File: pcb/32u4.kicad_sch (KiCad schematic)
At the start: 114 parts, among them J0 USB_C_Receptacle_USB2.0, SW00 SW_SPST, SW01 SW_SPST, SW010 SW_SPST, SW011 SW_SPST, SW02 SW_SPST, SW03 SW_SPST, SW04 SW_SPST, SW05 SW_SPST, SW06 SW_SPST, SW07 SW_SPST, SW08 SW_SPST, SW09 SW_SPST, SW1.0 SW_SPST, SW1.1 SW_SPST, SW110 SW_SPST, SW111 SW_SPST, SW12 SW_SPST, SW13 SW_SPST, SW14 SW_SPST, SW15 SW_SPST, SW16 SW_SPST, SW17 SW_SPST, SW18 SW_SPST, SW19 SW_SPST, SW20 SW_SPST, SW21 SW_SPST, SW210 SW_SPST, SW211 SW_SPST, SW22 SW_SPST, SW23 SW_SPST, SW24 SW_SPST, SW25 SW_SPST, SW26 SW_SPST, SW27 SW_SPST, SW28 SW_SPST, SW29 SW_SPST, SW30 SW_SPST, SW31 SW_SPST, SW310 SW_SPST, SW311 SW_SPST, SW32 SW_SPST, SW33 SW_SPST, SW34 SW_SPST, SW35 SW_SPST, SW36 SW_SPST, SW37 SW_SPST, SW38 SW_SPST, SW39 SW_SPST, SW40 SW_SPST, SW41 SW_SPST, SW411 SW_SPST, SW42 SW_SPST, SW44 SW_SPST, SW45 SW_SPST, SW46 SW_SPST, SW47 SW_SPST, SW49 SW_SPST, U0 ATmega32U4-A, U1 SRV05-4, Y0 Crystal_GND24_Small

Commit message: updated pcb to rp2040
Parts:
- removed C0, C1: 22pf, Capacitor_SMD:C_0805_2012Metric, symbol Device:C_Small
- removed C2: 1uf, Capacitor_SMD:C_0805_2012Metric, symbol Device:C_Small
- removed C3, C4, C6: .1uf / 100nf, Capacitor_SMD:C_0805_2012Metric, symbol Device:C_Small
- removed C5: 10uf, Capacitor_SMD:C_0805_2012Metric, symbol Device:C_Small
- removed F0: Polyfuse, Fuse:Fuse_1206_3216Metric, symbol Device:Polyfuse
- removed J0: USB_C_Receptacle_USB2.0, Connector_USB:USB_C_Receptacle_HRO_TYPE-C-31-M-12, symbol Connector:USB_C_Receptacle_USB2.0
- removed R0: 10k, Resistor_SMD:R_0805_2012Metric, symbol Device:R
- removed R1, R2: 22, Resistor_SMD:R_0805_2012Metric, symbol Device:R_Small
- removed R3, R4: 5.1k, Resistor_SMD:R_0805_2012Metric, symbol Device:R_Small
- removed R5: 10k, Resistor_SMD:R_0805_2012Metric, symbol Device:R_Small
- removed SWRESET1: SW_PUSH, Button_Switch_SMD:SW_SPST_TL3342, symbol keyboard_parts:SW_PUSH
- removed U0: ATmega32U4-A, Package_QFP:TQFP-44_10x10mm_P0.8mm, symbol MCU_Microchip_ATmega:ATmega32U4-A
- removed U1: SRV05-4, Package_TO_SOT_SMD:SOT-23-6, symbol Power_Protection:SRV05-4
- removed Y0: Crystal_GND24_Small, Crystal:Crystal_SMD_3225-4Pin_3.2x2.5mm, symbol Device:Crystal_GND24_Small
- renumbered D0506 to D506, SW010 to SW10, SW011 to SW11
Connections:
- no-connect marks 5 -> 1
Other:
- added sheet Rp2040  (rp2040_temp/RP2040_tmp.kicad_sch)

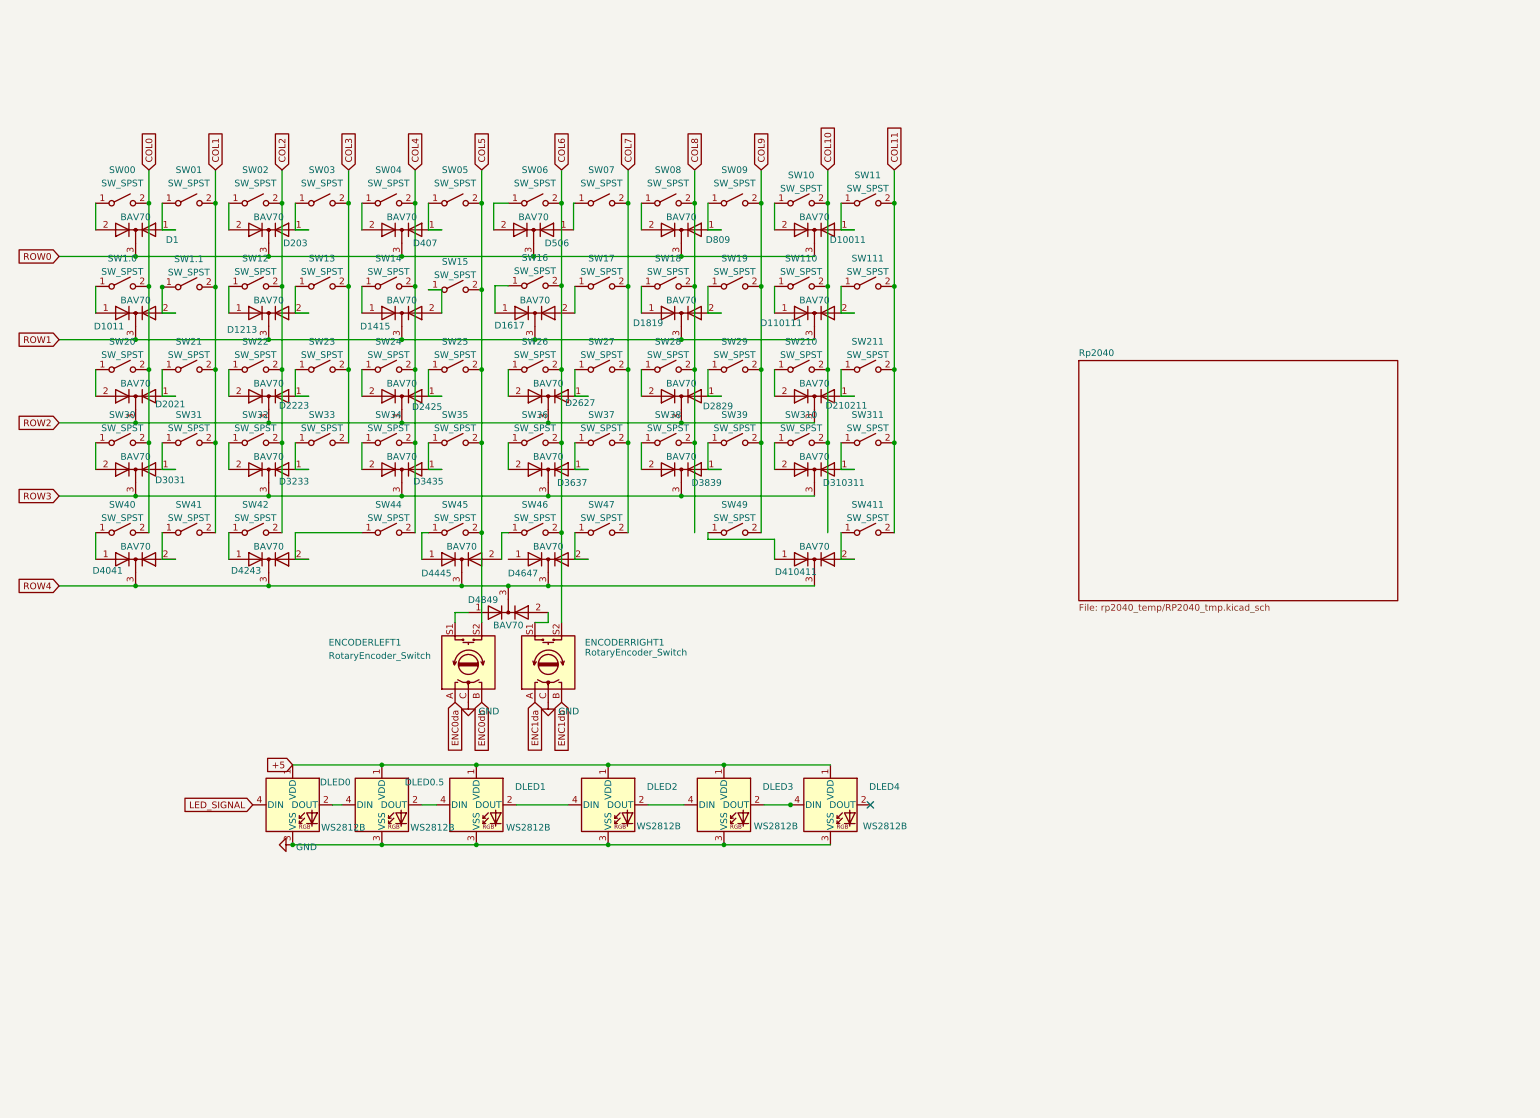
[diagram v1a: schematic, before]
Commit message: finalized placement and pcb
encoder and component placement was updated.
Further deleted backups from repo
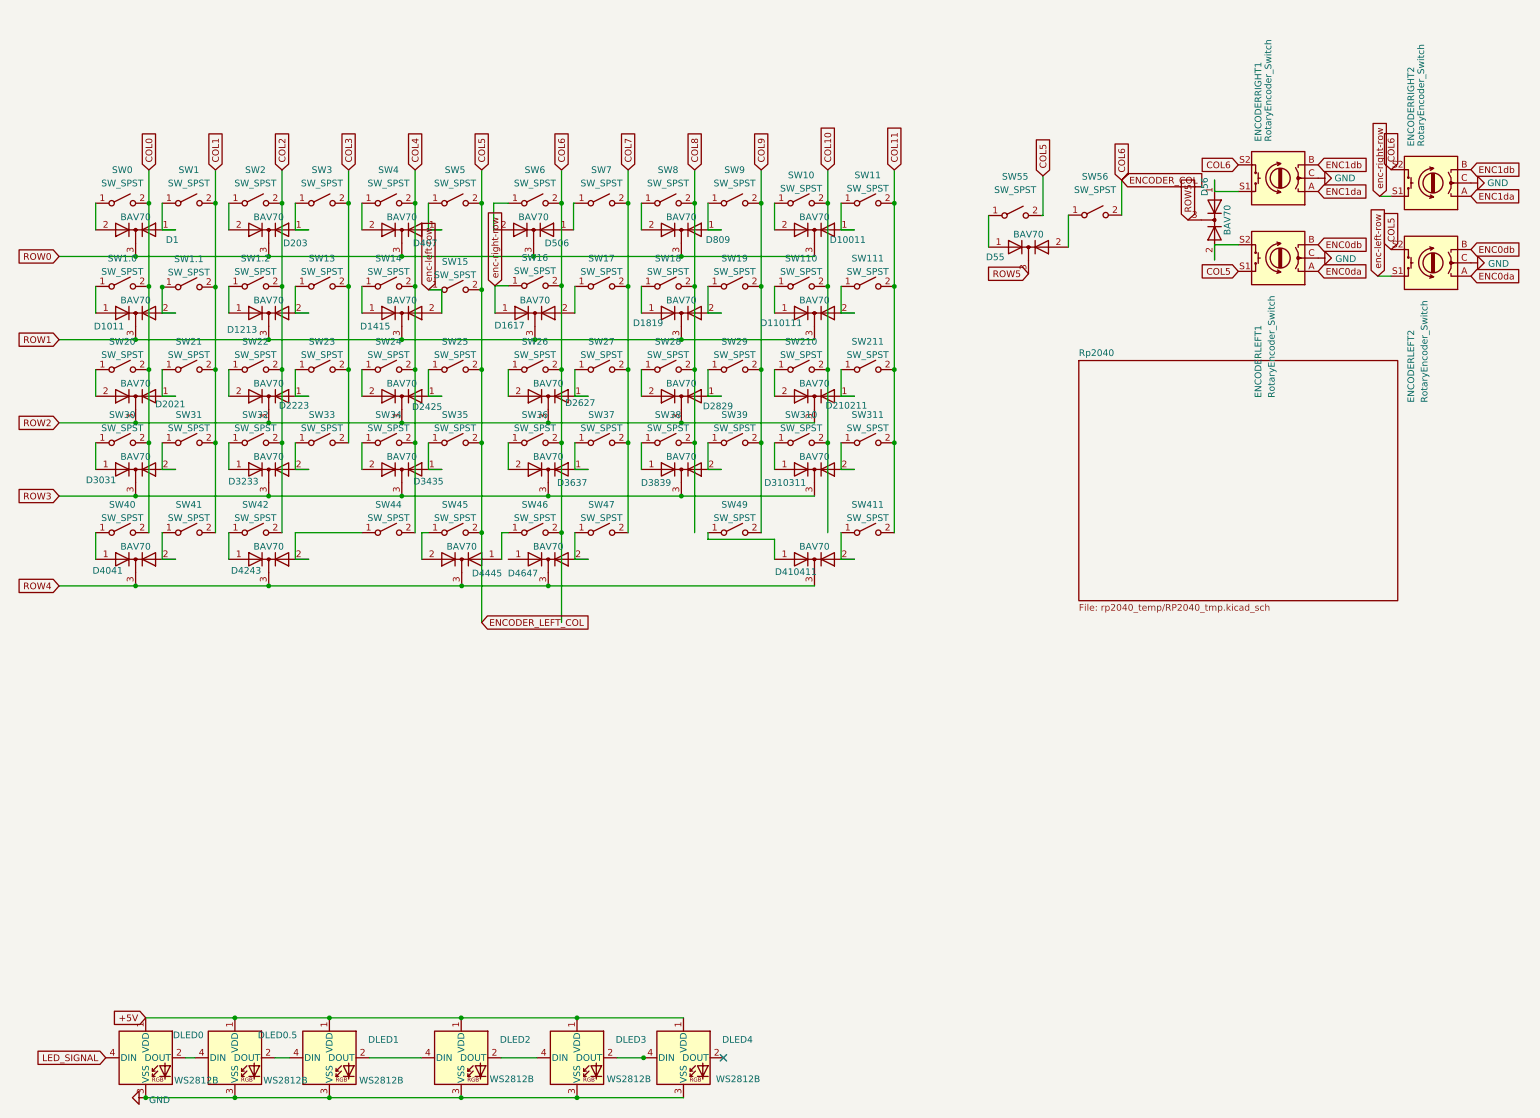
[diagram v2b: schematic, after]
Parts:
- removed D4849: BAV70, Package_TO_SOT_SMD:SOT-23, symbol Diode:BAV70
- added D55, D56: BAV70, Package_TO_SOT_SMD:SOT-23, symbol Diode:BAV70
- added ENCODERLEFT2, ENCODERRIGHT2: RotaryEncoder_Switch, Rotary_Encoder:RotaryEncoder_Alps_EC11E-Switch_Vertical_H20mm, symbol Device:RotaryEncoder_Switch
- added SW55, SW56: SW_SPST, Keebio-Parts:MX-Alps-Choc-1U-NoLED, symbol Switch:SW_SPST
- D1, D10011, D1011, D110111, D1213, D1415, D1617, D1819, D2021, D203, D210211, D2223, D2425, D2627, D2829, D3031, D310311, D3233, D3435, D3637, D3839, D4041, D407, D410411, D4243, D4445, D4647, D506, D809: LCSC (none) -> C68978
- SW0: renamed from SW00; footprint kbd:keyswitch_cherrymx_alps_combo_fixed -> Keebio-Parts:MX-Alps-Choc-1U-NoLED
- SW1: renamed from SW01; footprint kbd:keyswitch_cherrymx_alps_combo_fixed -> Keebio-Parts:MX-Alps-Choc-1U-NoLED
- SW1.0, SW1.1, SW10, SW11, SW110, SW111, SW13, SW14, SW15, SW16, SW17, SW18, SW19, SW20, SW21, SW210, SW211, SW22, SW23, SW24, SW25, SW26, SW27, SW28, SW29, SW30, SW31, SW310, SW311, SW32, SW33, SW34, SW35, SW36, SW37, SW38, SW39, SW40, SW41, SW411, SW42, SW44, SW45, SW46, SW47, SW49: footprint kbd:keyswitch_cherrymx_alps_combo_fixed -> Keebio-Parts:MX-Alps-Choc-1U-NoLED
- SW1.2: renamed from SW12; footprint kbd:keyswitch_cherrymx_alps_combo_fixed -> Keebio-Parts:MX-Alps-Choc-1U-NoLED
- SW2: renamed from SW02; footprint kbd:keyswitch_cherrymx_alps_combo_fixed -> Keebio-Parts:MX-Alps-Choc-1U-NoLED
- SW3: renamed from SW03; footprint kbd:keyswitch_cherrymx_alps_combo_fixed -> Keebio-Parts:MX-Alps-Choc-1U-NoLED
- SW4: renamed from SW04; footprint kbd:keyswitch_cherrymx_alps_combo_fixed -> Keebio-Parts:MX-Alps-Choc-1U-NoLED
- SW5: renamed from SW05; footprint kbd:keyswitch_cherrymx_alps_combo_fixed -> Keebio-Parts:MX-Alps-Choc-1U-NoLED
- SW6: renamed from SW06; footprint kbd:keyswitch_cherrymx_alps_combo_fixed -> Keebio-Parts:MX-Alps-Choc-1U-NoLED
- SW7: renamed from SW07; footprint kbd:keyswitch_cherrymx_alps_combo_fixed -> Keebio-Parts:MX-Alps-Choc-1U-NoLED
- SW8: renamed from SW08; footprint kbd:keyswitch_cherrymx_alps_combo_fixed -> Keebio-Parts:MX-Alps-Choc-1U-NoLED
- SW9: renamed from SW09; footprint kbd:keyswitch_cherrymx_alps_combo_fixed -> Keebio-Parts:MX-Alps-Choc-1U-NoLED
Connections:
- net COL5: now also ENCODERLEFT1.S1, ENCODERLEFT2.S2, SW55.2 (B); no longer ENCODERLEFT1.S2
- net COL6: now also ENCODERRIGHT2.S2, SW56.2 (B)
- net ENC0da: now also ENCODERLEFT2.A
- net ENC0db: now also ENCODERLEFT2.B
- net ENC1da: now also ENCODERRIGHT2.A
- net ENC1db: now also ENCODERRIGHT2.B
- net GND: now also ENCODERLEFT2.C, ENCODERRIGHT2.C
- net enc-right-row: now reaches D1617.1 (A), SW16.1 (A)
- net enc-right-row: now also ENCODERRIGHT2.S1
- net at SW46.1 (A): now also D4445.1 (A); no longer D4445.2 (A)
- net at SW311.1 (A): now also D310311.2 (A); no longer D310311.1 (A)
- net at ENCODERRIGHT1.S1: now also D56.1 (A)
- net at SW31.1 (A): now also D3031.2 (A); no longer D3031.1 (A)
- net enc-left-row: now reaches D1415.2 (A), SW15.1 (A)
- net enc-left-row: now also ENCODERLEFT2.S1
- net at SW33.1 (A): now also D3233.2 (A); no longer D3233.1 (A)
- net at SW310.1 (A): now also D310311.1 (A); no longer D310311.2 (A)
- net at SW32.1 (A): now also D3233.1 (A); no longer D3233.2 (A)
- net at SW39.1 (A): now also D3839.2 (A); no longer D3839.1 (A)
- net at SW38.1 (A): now also D3839.1 (A); no longer D3839.2 (A)
- net at SW30.1 (A): now also D3031.1 (A); no longer D3031.2 (A)
- net at SW45.1 (A): now also D4445.2 (A); no longer D4445.1 (A)
- net +5 renamed +5V
- new net: D55.1 (A), SW55.1 (A)
- new net: D56.2 (A), ENCODERLEFT1.S2
- new net: D55.2 (A), SW56.1 (A)
- new net ROW5: D55.3 (K), D56.3 (K)
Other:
- moved on the sheet: DLED0, DLED0.5, DLED1, DLED2, DLED3, DLED4, ENCODERLEFT1, ENCODERRIGHT1
